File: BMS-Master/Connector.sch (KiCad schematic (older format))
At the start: 115 parts

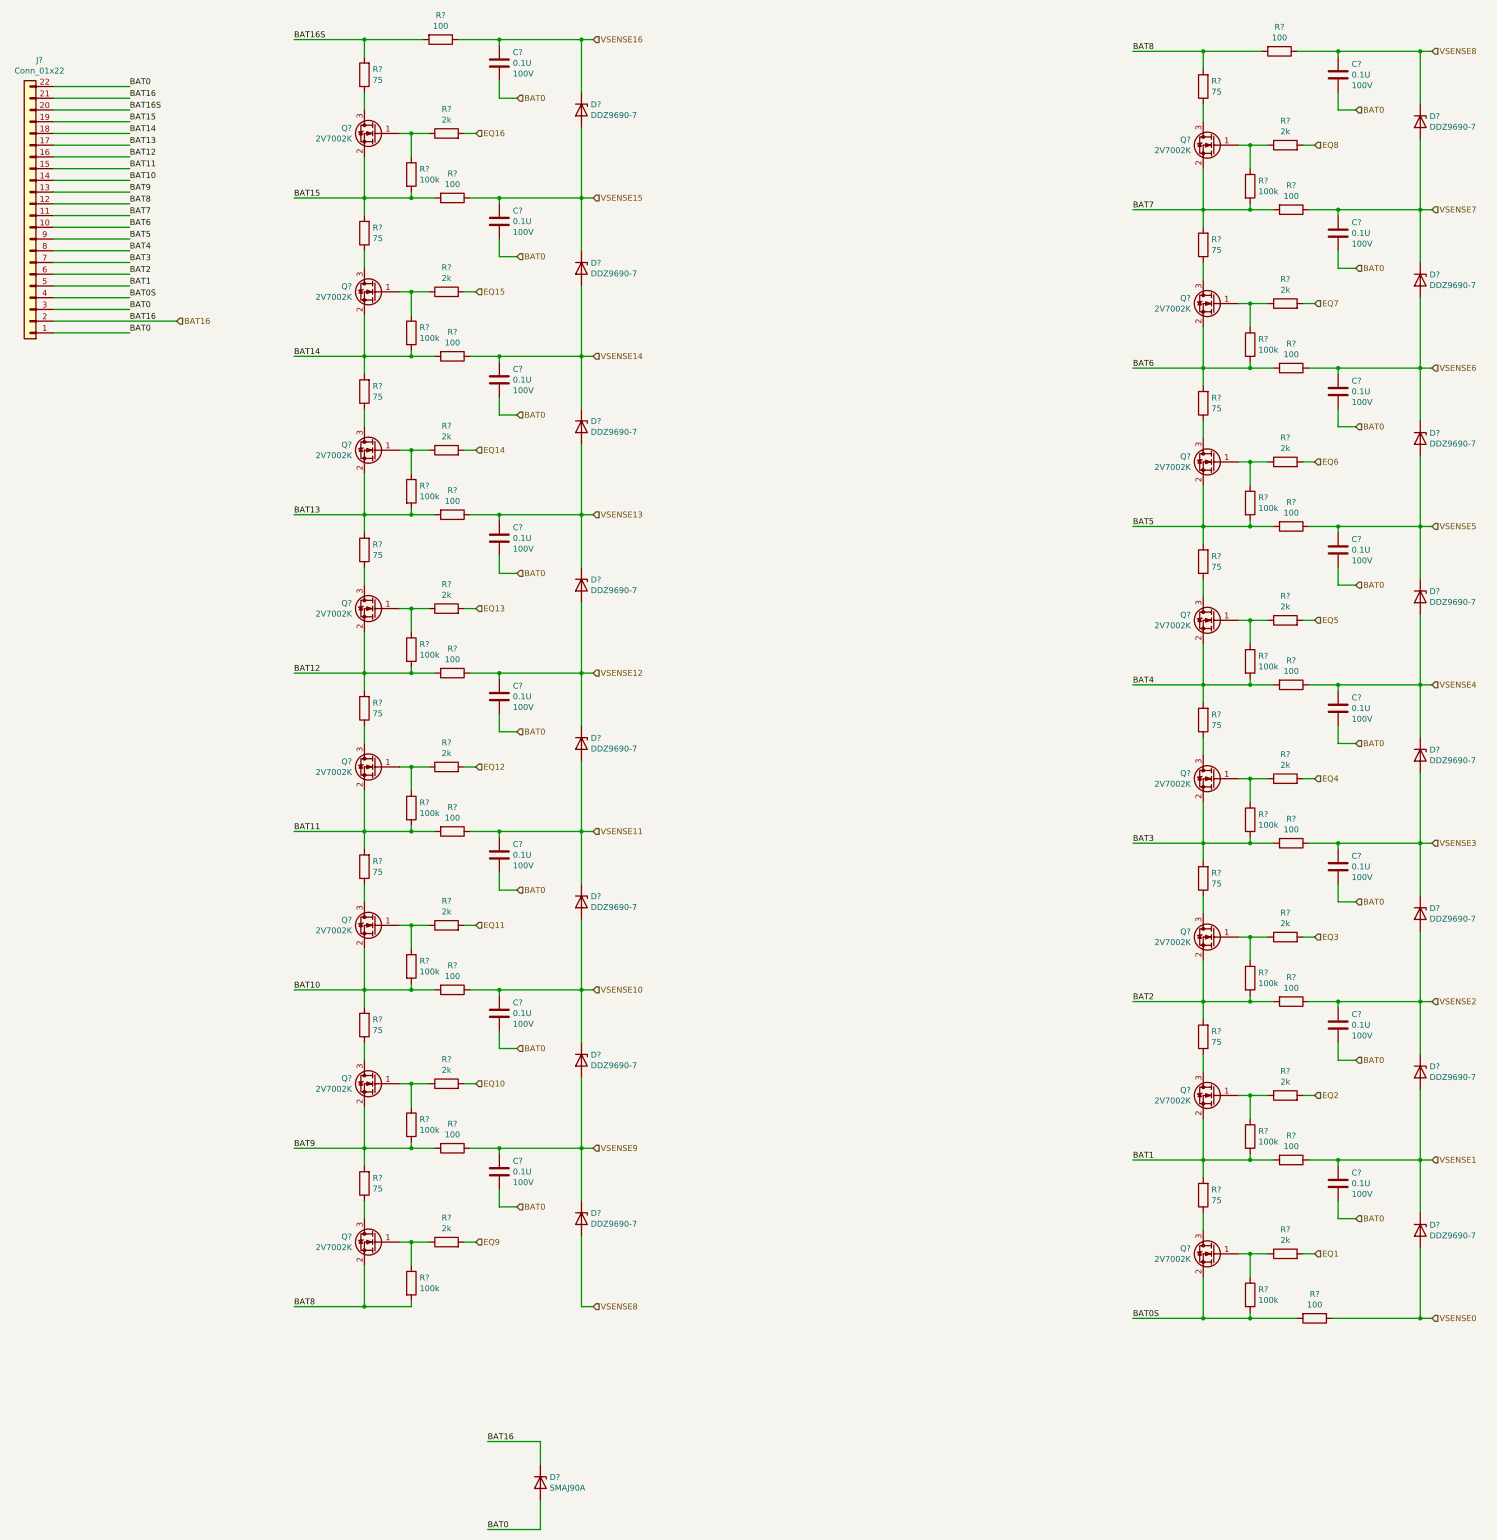
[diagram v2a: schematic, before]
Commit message: schematic update
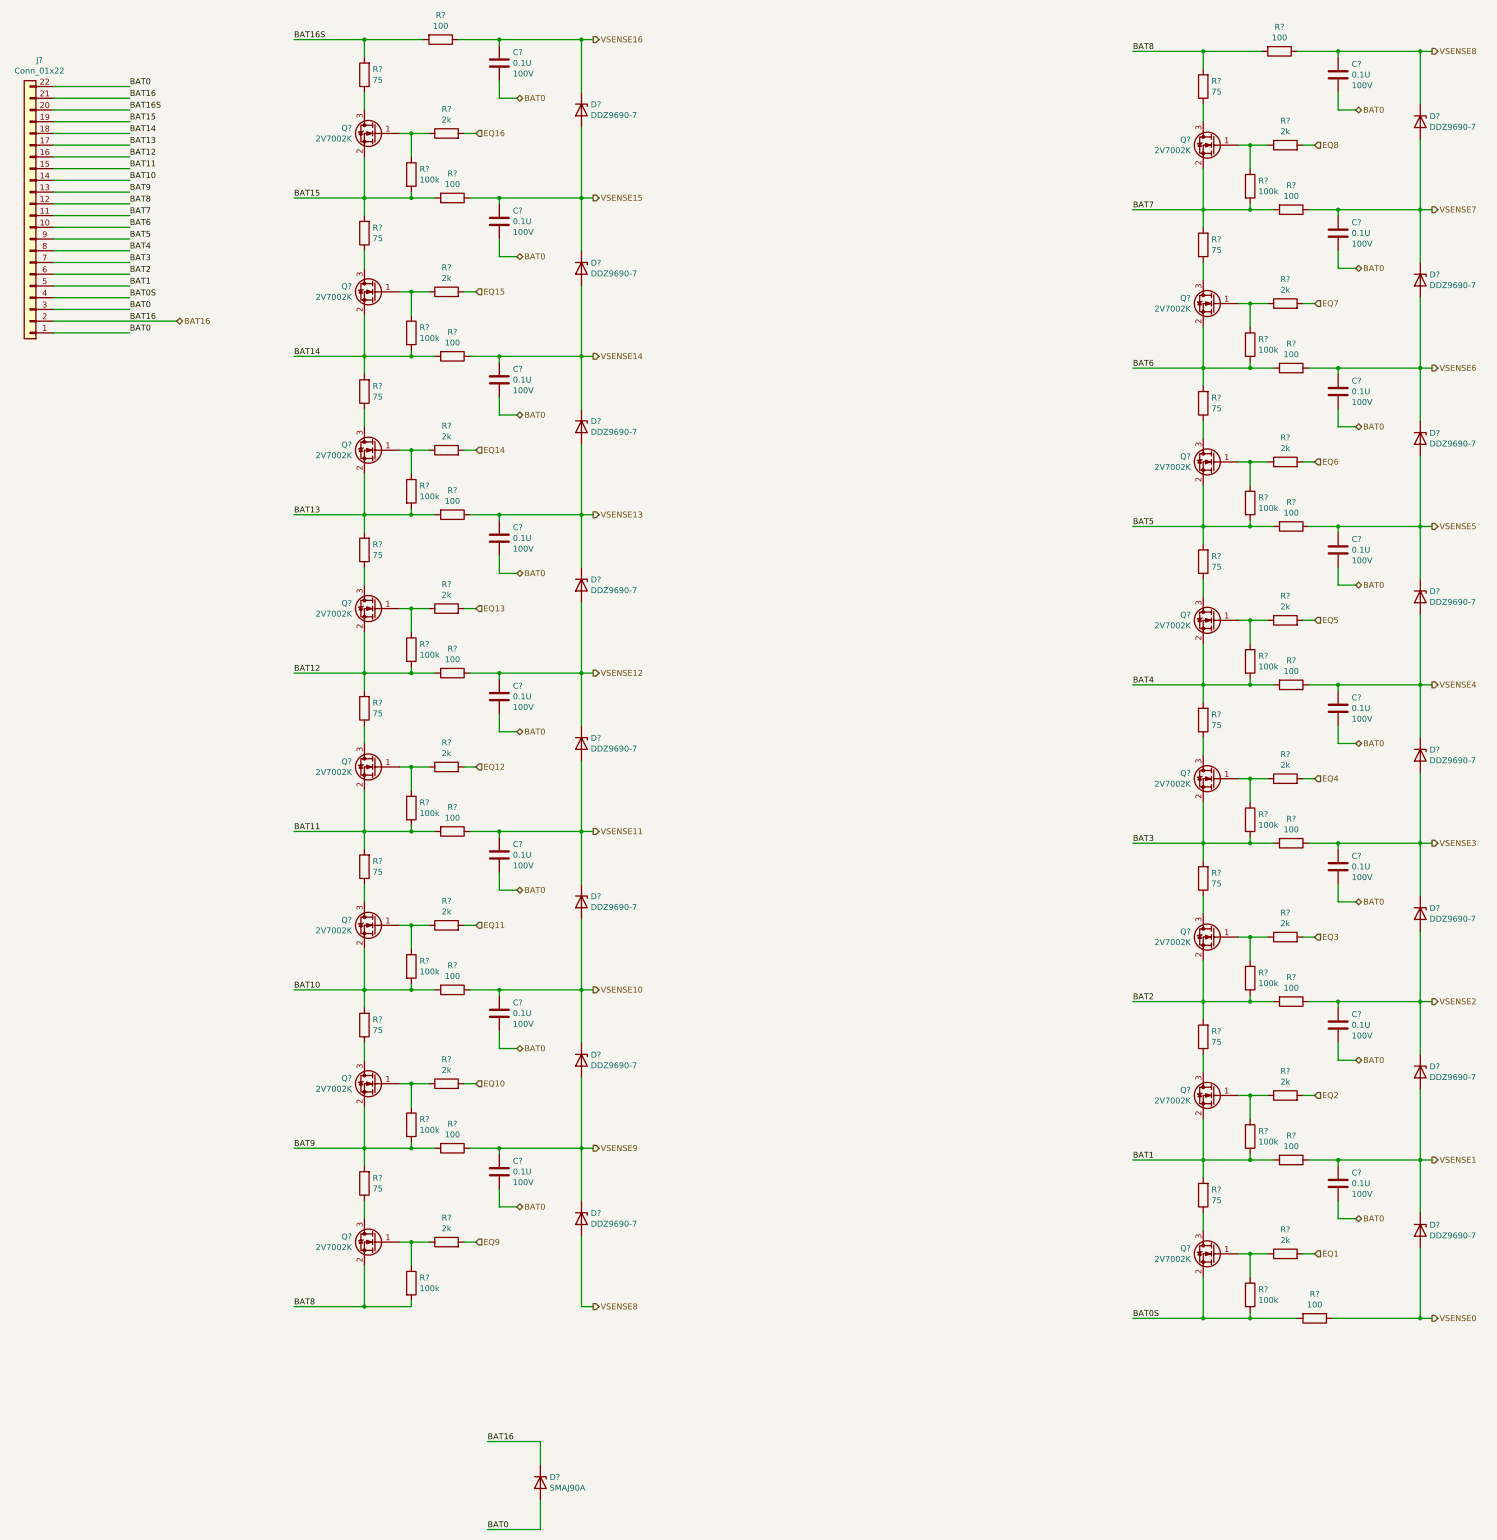
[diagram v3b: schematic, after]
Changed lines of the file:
@@
 $Descr A2 23386 16535
 encoding utf-8
-Sheet 2 6
+Sheet 2 8
 Title "BMS-Master"
 Date ""
@@
 Comment4 ""
 $EndDescr
-Text HLabel 5850 1500 2    50   Input ~ 0
+Text HLabel 5850 1500 2    50   Output ~ 0
 VSENSE16
-Text HLabel 5850 2850 2    50   Input ~ 0
+Text HLabel 5850 2850 2    50   Output ~ 0
 VSENSE15
 $Comp
@@
 	5050 1500 5750 1500
 Connection ~ 5750 1500
-Text HLabel 5200 2000 2    50   Input ~ 0
+Text HLabel 5200 2000 2    50   BiDi ~ 0
 BAT0
 Wire Wire Line
@@
 	-1   0    0    1
 $EndComp
-Text HLabel 5850 4200 2    50   Input ~ 0
+Text HLabel 5850 4200 2    50   Output ~ 0
 VSENSE14
 $Comp
@@
 Wire Wire Line
 	5050 2900 5050 2850
-Text HLabel 5200 3350 2    50   Input ~ 0
+Text HLabel 5200 3350 2    50   BiDi ~ 0
 BAT0
 Wire Wire Line
@@
 Wire Wire Line
 	5050 2850 5750 2850
-Text HLabel 5850 5550 2    50   Input ~ 0
+Text HLabel 5850 5550 2    50   Output ~ 0
 VSENSE13
 $Comp
@@
 Wire Wire Line
 	5050 4250 5050 4200
-Text HLabel 5200 4700 2    50   Input ~ 0
+Text HLabel 5200 4700 2    50   BiDi ~ 0
 BAT0
 Wire Wire Line
@@
 Text Label 3300 5550 0    50   ~ 0
 BAT13
-Text HLabel 5850 6900 2    50   Input ~ 0
+Text HLabel 5850 6900 2    50   Output ~ 0
 VSENSE12
 $Comp
@@
 Wire Wire Line
 	5050 5600 5050 5550
-Text HLabel 5200 6050 2    50   Input ~ 0
+Text HLabel 5200 6050 2    50   BiDi ~ 0
 BAT0
 Wire Wire Line
@@
 Wire Wire Line
 	5050 4200 5750 4200
-Text HLabel 5850 8250 2    50   Input ~ 0
+Text HLabel 5850 8250 2    50   Output ~ 0
 VSENSE11
 $Comp
@@
 Wire Wire Line
 	5050 6950 5050 6900
-Text HLabel 5200 7400 2    50   Input ~ 0
+Text HLabel 5200 7400 2    50   BiDi ~ 0
 BAT0
 Wire Wire Line
@@
 Text Label 3300 8250 0    50   ~ 0
 BAT11
-Text HLabel 5850 9600 2    50   Input ~ 0
+Text HLabel 5850 9600 2    50   Output ~ 0
 VSENSE10
 $Comp
@@
 Wire Wire Line
 	5050 8300 5050 8250
-Text HLabel 5200 8750 2    50   Input ~ 0
+Text HLabel 5200 8750 2    50   BiDi ~ 0
 BAT0
 Wire Wire Line
@@
 Wire Wire Line
 	5050 8250 5750 8250
-Text HLabel 5850 10950 2    50   Input ~ 0
+Text HLabel 5850 10950 2    50   Output ~ 0
 VSENSE9
 $Comp
@@
 Wire Wire Line
 	5050 9650 5050 9600
-Text HLabel 5200 10100 2    50   Input ~ 0
+Text HLabel 5200 10100 2    50   BiDi ~ 0
 BAT0
 Wire Wire Line
@@
 Text Label 3300 10950 0    50   ~ 0
 BAT9
-Text HLabel 5850 12300 2    50   Input ~ 0
+Text HLabel 5850 12300 2    50   Output ~ 0
 VSENSE8
 $Comp
@@
 Wire Wire Line
 	5050 11000 5050 10950
-Text HLabel 5200 11450 2    50   Input ~ 0
+Text HLabel 5200 11450 2    50   BiDi ~ 0
 BAT0
 Wire Wire Line
@@
 Wire Wire Line
 	5050 6900 5750 6900
-Text HLabel 13000 1600 2    50   Input ~ 0
+Text HLabel 13000 1600 2    50   Output ~ 0
 VSENSE8
-Text HLabel 13000 2950 2    50   Input ~ 0
+Text HLabel 13000 2950 2    50   Output ~ 0
 VSENSE7
 $Comp
@@
 	12200 1600 12900 1600
 Connection ~ 12900 1600
-Text HLabel 12350 2100 2    50   Input ~ 0
+Text HLabel 12350 2100 2    50   BiDi ~ 0
 BAT0
 Wire Wire Line
@@
 Text Label 10450 2950 0    50   ~ 0
 BAT7
-Text HLabel 13000 4300 2    50   Input ~ 0
+Text HLabel 13000 4300 2    50   Output ~ 0
 VSENSE6
 $Comp
@@
 Wire Wire Line
 	12200 3000 12200 2950
-Text HLabel 12350 3450 2    50   Input ~ 0
+Text HLabel 12350 3450 2    50   BiDi ~ 0
 BAT0
 Wire Wire Line
@@
 Wire Wire Line
 	12200 2950 12900 2950
-Text HLabel 13000 5650 2    50   Input ~ 0
+Text HLabel 13000 5650 2    50   Output ~ 0
 VSENSE5
 $Comp
@@
 Wire Wire Line
 	12200 4350 12200 4300
-Text HLabel 12350 4800 2    50   Input ~ 0
+Text HLabel 12350 4800 2    50   BiDi ~ 0
 BAT0
 Wire Wire Line
@@
 Text Label 10450 5650 0    50   ~ 0
 BAT5
-Text HLabel 13000 7000 2    50   Input ~ 0
+Text HLabel 13000 7000 2    50   Output ~ 0
 VSENSE4
 $Comp
@@
 Wire Wire Line
 	12200 5700 12200 5650
-Text HLabel 12350 6150 2    50   Input ~ 0
+Text HLabel 12350 6150 2    50   BiDi ~ 0
 BAT0
 Wire Wire Line
@@
 Wire Wire Line
 	12200 4300 12900 4300
-Text HLabel 13000 8350 2    50   Input ~ 0
+Text HLabel 13000 8350 2    50   Output ~ 0
 VSENSE3
 $Comp
@@
 Wire Wire Line
 	12200 7050 12200 7000
-Text HLabel 12350 7500 2    50   Input ~ 0
+Text HLabel 12350 7500 2    50   BiDi ~ 0
 BAT0
 Wire Wire Line
@@
 Text Label 10450 8350 0    50   ~ 0
 BAT3
-Text HLabel 13000 9700 2    50   Input ~ 0
+Text HLabel 13000 9700 2    50   Output ~ 0
 VSENSE2
 $Comp
@@
 Wire Wire Line
 	12200 8400 12200 8350
-Text HLabel 12350 8850 2    50   Input ~ 0
+Text HLabel 12350 8850 2    50   BiDi ~ 0
 BAT0
 Wire Wire Line
@@
 Wire Wire Line
 	12200 8350 12900 8350
-Text HLabel 13000 11050 2    50   Input ~ 0
+Text HLabel 13000 11050 2    50   Output ~ 0
 VSENSE1
 $Comp
@@
 Wire Wire Line
 	12200 9750 12200 9700
-Text HLabel 12350 10200 2    50   Input ~ 0
+Text HLabel 12350 10200 2    50   BiDi ~ 0
 BAT0
 Wire Wire Line
@@
 Text Label 10450 11050 0    50   ~ 0
 BAT1
-Text HLabel 13000 12400 2    50   Input ~ 0
+Text HLabel 13000 12400 2    50   Output ~ 0
 VSENSE0
 $Comp
@@
 Wire Wire Line
 	12200 11100 12200 11050
-Text HLabel 12350 11550 2    50   Input ~ 0
+Text HLabel 12350 11550 2    50   BiDi ~ 0
 BAT0
 Wire Wire Line
@@
 Text Label 1900 4000 0    50   ~ 0
 BAT0
-Text HLabel 2300 3900 2    50   Input ~ 0
+Text HLabel 2300 3900 2    50   BiDi ~ 0
 BAT16
 Wire Wire Line
